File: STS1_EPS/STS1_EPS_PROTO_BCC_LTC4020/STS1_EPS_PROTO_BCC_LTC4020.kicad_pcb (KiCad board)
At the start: 2 copper layers, 47 parts, among them J1 1729267, J10 External Thermistor, J11 Terminal BAT, J9 Output, Q1 SI7135DP-T1-GE3, U1 LTC4020EUHF-PBF, U2 SI7272DP-T1-GE3, U3 SI7272DP-T1-GE3

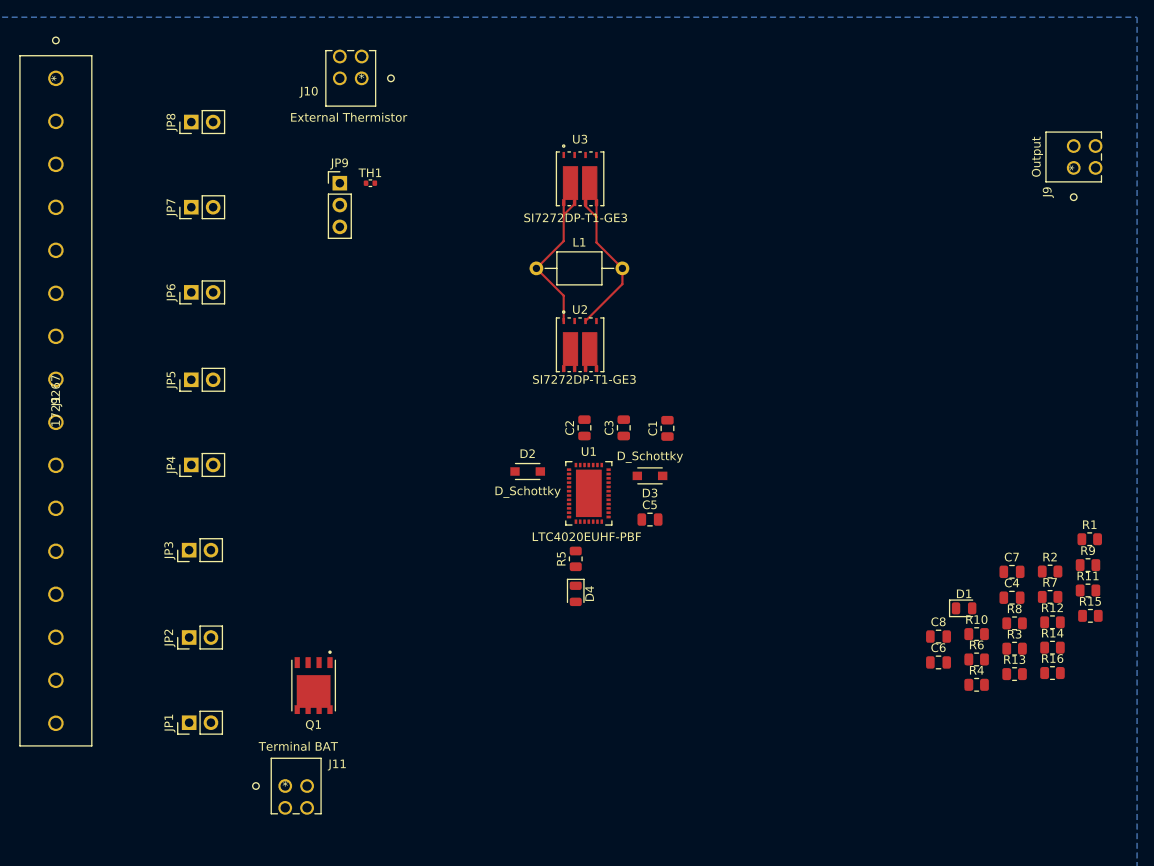
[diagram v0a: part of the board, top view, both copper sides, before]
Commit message: Re-added battery charger schematic for STS1_EPS_PROTO_BCC_LTC4020 project.
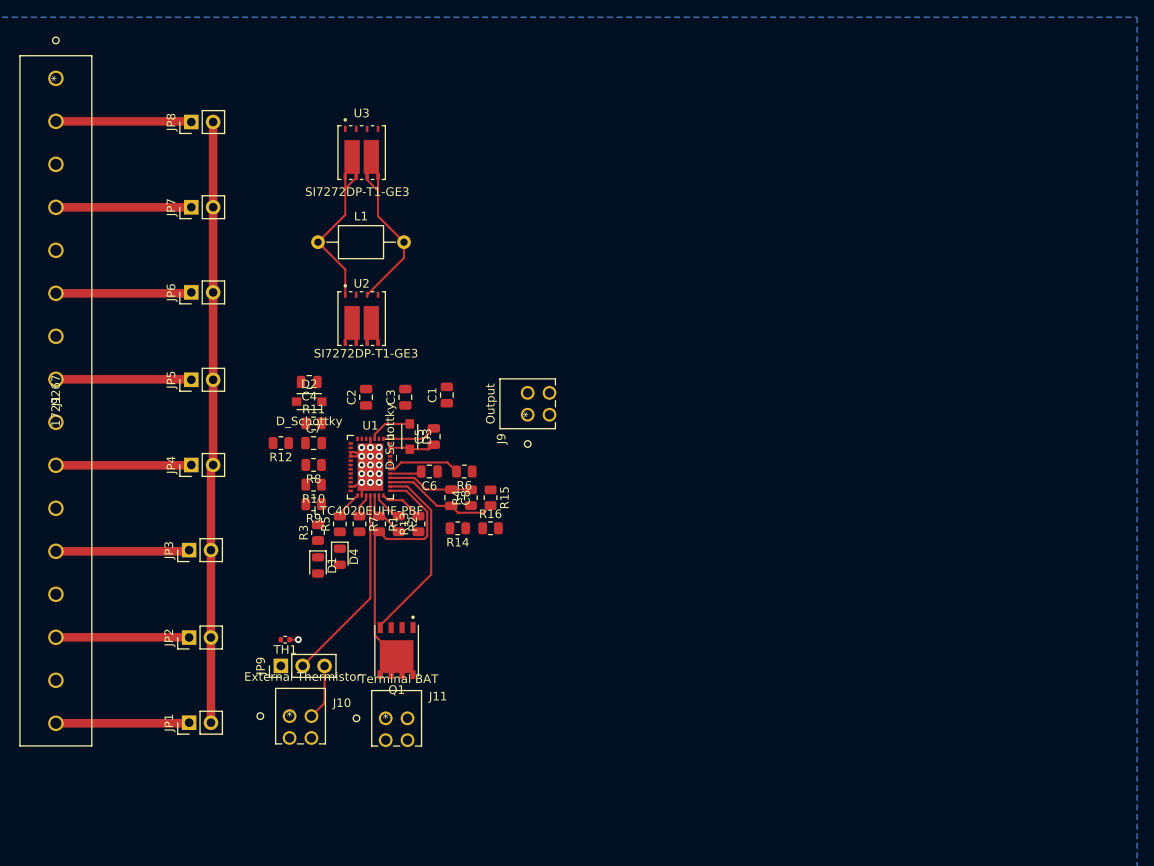
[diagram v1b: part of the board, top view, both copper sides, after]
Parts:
- moved R11 92.1 mm to (91.9, 73.7)
- moved R12 92.1 mm to (88.1, 75.9), turned to 180 degrees
- moved R9 90.3 mm to (91.9, 83.1), turned to 180 degrees
- moved C4 85.5 mm to (91.4, 68.8), turned to 180 degrees
- moved R8 83.6 mm to (91.9, 78.5), turned to 180 degrees
- moved R1 82.7 mm to (99.6, 85.3), turned to 270 degrees
- moved C7 82.6 mm to (91.9, 75.9)
- moved R3 82.1 mm to (92.5, 86.4), turned to 90 degrees
- moved R7 80.8 mm to (97.3, 85.3), turned to 270 degrees
- moved R10 79.0 mm to (91.9, 80.8), turned to 180 degrees
- moved R2 75.9 mm to (101.9, 85.3), turned to 270 degrees
- moved D1 75.3 mm to (92.5, 90.2), turned to 270 degrees
- moved J10 74.6 mm to (89.2, 107.7), turned to 0 degrees
- moved R13 71.5 mm to (104.1, 85.3), turned to 90 degrees
- moved R15 71.1 mm to (112.5, 82.3), turned to 270 degrees
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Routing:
- net /EPS Battery Charger/Vin: track 0.00 -> 70.0 mm
- net /EPS Battery Charger/BAT: track 0.00 -> 31.8 mm
- net /EPS Battery Charger/NTC: track 0.00 -> 23.1 mm
- net /EPS Battery Charger/BGATE: track 0.00 -> 22.0 mm
- net Net-(J1-Pad10): track 0.00 -> 15.8 mm
- net Net-(J1-Pad4): track 0.02 -> 15.8 mm
- net Net-(J1-Pad8): track 0.07 -> 15.8 mm
- net Net-(J1-Pad2): track 0.11 -> 15.8 mm
- net Net-(J1-Pad6): track 0.15 -> 15.8 mm
- net GND: track 0.00 -> 15.6 mm, vias 0 -> 16
- net Net-(J1-Pad12): track 0.00 -> 15.6 mm
- net Net-(J1-Pad16): track 0.00 -> 15.5 mm
- net Net-(J1-Pad14): track 0.00 -> 15.5 mm
- net /EPS Battery Charger/CSN: track 0.00 -> 13.5 mm
- net /EPS Battery Charger/CSP: track 0.00 -> 9.97 mm
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
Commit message: Worked on STS1_EPS_PROTO_BCC_LTC4020 pcb.
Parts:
- moved R16 7.62 mm to (108.0, 91.9), turned to 270 degrees
- moved R15 6.04 mm to (110.2, 87.9), turned to 90 degrees
- moved C1 2.55 mm to (104.9, 70.6)
- moved C2 2.29 mm to (100.3, 70.6)
- moved R14 2.17 mm to (108.0, 87.9), turned to 90 degrees
- moved D3 1.30 mm to (104.4, 74.9)
- moved C5 1.30 mm to (107.2, 74.9)
- moved C6 0.51 mm to (105.4, 78.7)
- moved R6 0.51 mm to (109.5, 78.7)
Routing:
- net /EPS Battery Charger/VFB: track 5.65 -> 23.1 mm, vias 0 -> 2
- net /EPS Battery Charger/Vout: track 0.00 -> 12.6 mm, vias 0 -> 2
- net /EPS Battery Charger/SW2: track 25.4 -> 19.0 mm
- net GND: track 15.6 -> 21.9 mm, vias 16 -> 20
- net /EPS Battery Charger/CSP: track 9.97 -> 16.2 mm, vias 0 -> 2
- net /EPS Battery Charger/VFBMAX: track 5.08 -> 10.8 mm, vias 0 -> 2
- net /EPS Battery Charger/BST2: track 5.36 -> 0.00 mm
- net /EPS Battery Charger/INTVCC: track 5.09 -> 0.00 mm
- net Net-(Q1-Pad1): track 0.00 -> 5.01 mm
- net /EPS Battery Charger/BAT: track 31.8 -> 36.7 mm
- net /EPS Battery Charger/CSN: track 13.5 -> 12.9 mm

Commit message: Reworked BCC
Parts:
- removed J10: External Thermistor, footprints:1725656
- added C10: 56µ, Capacitor_SMD:C_Elec_6.3x5.4, F.Cu at (89.7, 38.9)
- added C9: 56µ, Capacitor_SMD:C_Elec_6.3x5.4, F.Cu at (98.6, 38.9)
- added J4: External NTC, footprints:1725656, F.Cu at (89.4, 108.0)
- C1, C7: value C -> 100n; footprint Capacitor_SMD:C_0805_2012Metric -> Capacitor_SMD:C_1812_4532Metric
- C2: value C -> 4µ7; footprint Capacitor_SMD:C_0805_2012Metric -> Capacitor_SMD:C_1812_4532Metric
- C3: value CP -> 56µ; footprint Capacitor_SMD:C_0805_2012Metric -> Capacitor_SMD:C_Elec_6.3x5.4
- C4, C5: value C -> 1µ
- L1: value 1m -> INDUCTOR
- R11, R12: value R -> 5m; footprint Resistor_SMD:R_0805_2012Metric -> footprints:CST0612-FC-R002E
- TH1: footprint Resistor_SMD:R_0402_1005Metric -> Resistor_SMD:R_0603_1608Metric
- moved J2 32.5 mm to (116.6, 40.1)
- moved C3 32.1 mm to (107.2, 38.9)
- moved C7 26.9 mm to (91.2, 49.0), turned to 180 degrees
- moved R11 24.1 mm to (113.5, 63.0), turned to 90 degrees
- moved C1 22.9 mm to (106.4, 47.8), turned to 180 degrees
- moved R12 22.6 mm to (91.2, 53.6), turned to 0 degrees
- moved C2 18.3 mm to (106.4, 53.3), turned to 180 degrees
- moved U3 17.9 mm to (91.2, 58.9), turned to 180 degrees
- moved L1 12.4 mm to (98.3, 63.5), turned to 90 degrees
- moved U2 8.52 mm to (105.7, 58.9), turned to 180 degrees
- moved R8 4.99 mm to (87.1, 79.8), turned to 90 degrees
- moved C5 3.09 mm to (104.1, 75.4)
- moved R14 2.54 mm to (110.5, 87.9)
- moved R16 2.54 mm to (110.5, 91.9)
- moved D3 2.29 mm to (106.7, 74.9)
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- renumbered J9 to J2, J11 to J3
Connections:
- C7 pad 2: /EPS Battery Charger/SENSBOT -> Net-(C7-Pad2)
- R11 pad 2: /EPS Battery Charger/SENSTOP -> /EPS Battery Charger/Vin
- R12 pad 1: /EPS Battery Charger/SENSBOT -> Net-(C7-Pad2)
- R12 pad 2: GND -> /EPS Battery Charger/SENSBOT
- U1 pad 28: Net-(U1-Pad28) -> /EPS Battery Charger/Vin
- U1 pad 29: Net-(U1-Pad29) -> GND
- U2 pad 7: /EPS Battery Charger/SENSTOP -> Net-(R11-Pad3)
- U2 pad 8: Net-(U2-Pad8) -> Net-(R11-Pad3)
- U3 pad 1: /EPS Battery Charger/SENSBOT -> Net-(C7-Pad2)
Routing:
- net /EPS Battery Charger/Vin: track 70.0 -> 129.6 mm, vias 0 -> 5
- net GND: track 21.9 -> 74.1 mm, vias 20 -> 37
- net /EPS Battery Charger/BG2: track 0.00 -> 34.1 mm, vias 0 -> 2
- net /EPS Battery Charger/Vout: track 12.6 -> 45.2 mm
- net /EPS Battery Charger/BG1: track 0.00 -> 29.6 mm, vias 0 -> 2
- net /EPS Battery Charger/SENSBOT: track 0.00 -> 26.7 mm, vias 0 -> 2
- net /EPS Battery Charger/TG2: track 0.00 -> 22.8 mm, vias 0 -> 2
- net /EPS Battery Charger/TG1: track 0.00 -> 22.0 mm, vias 0 -> 2
- net /EPS Battery Charger/INTVCC: track 0.00 -> 14.6 mm, vias 0 -> 3
- net /EPS Battery Charger/SW1: track 18.3 -> 31.1 mm, vias 0 -> 3
- net Net-(R10-Pad1): track 0.00 -> 11.3 mm
- net Net-(Q1-Pad1): track 5.01 -> 15.5 mm
- net /EPS Battery Charger/BAT: track 36.7 -> 46.5 mm
- net /EPS Battery Charger/BST1: track 0.00 -> 9.80 mm
- net Net-(R9-Pad1): track 0.00 -> 9.56 mm, vias 0 -> 2
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- added copper zone on F.Cu, net /EPS Battery Charger/Vout
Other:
- board outline added: 63 x 81.3 mm
- net class 6A Power added: clearance 0.2, trace_width 0.25, via_dia 0.8, via_drill 0.4

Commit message: - STS1_EPS_PROTO_SCC_L6920 now uses the STS1 PCB template and is again ready for review. - WOrked on STS1_EPS_PROTO_BCC_LTC4020.
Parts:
- removed the C1 at (106.4, 47.8)
- removed the C10 at (89.7, 38.9)
- removed the C2 at (106.4, 53.3)
- removed the C3 at (107.2, 38.9)
- removed the C9 at (98.6, 38.9)
- added C1: 680µ, Capacitor_Tantalum_SMD:CP_EIA-7361-438_AVX-U, F.Cu at (289.9, 153.6)
- added C1: 100n, Capacitor_SMD:C_1812_4532Metric, F.Cu at (232.2, 128.4)
- added C10: 680p, Capacitor_SMD:C_0805_2012Metric, F.Cu at (291.7, 178.0)
- added C10: 56µ, Capacitor_SMD:C_Elec_6.3x5.4, F.Cu at (224.4, 121.9)
- added C11: 50µ, footprints:FE52N6J0506KB, F.Cu at (223.5, 78.4)
- added C12: 50µ, footprints:FE52N6J0506KB, F.Cu at (217.3, 20.7)
- added C13: 2µ2, Capacitor_SMD:C_0805_2012Metric, F.Cu at (304.9, 59.0)
- added C14: 10µ, Capacitor_SMD:C_0805_2012Metric, F.Cu at (297.7, 68.5)
- added C15: 200n, Capacitor_SMD:C_0805_2012Metric, F.Cu at (299.3, 64.3)
- added C16: 680p, Capacitor_SMD:C_0805_2012Metric, F.Cu at (287.2, 178.0)
- added C2: 100n, Capacitor_SMD:C_0805_2012Metric, F.Cu at (316.1, 91.6)
- added C2: 4µ7, Capacitor_SMD:C_1812_4532Metric, F.Cu at (222.9, 142.8)
- added C3: 680µ, Capacitor_Tantalum_SMD:CP_EIA-7361-438_AVX-U, F.Cu at (273.8, 153.6)
- added C3: 56µ, Capacitor_SMD:C_Elec_6.3x5.4, F.Cu at (234.3, 121.9)
- added C9: 100n, Capacitor_SMD:C_0805_2012Metric, F.Cu at (299.4, 91.6)
- added C9: 56µ, Capacitor_SMD:C_Elec_6.3x5.4, F.Cu at (244.3, 121.9)
- added CON1: DISCO-CON1, footprints:Cubesatconnector, B.Cu at (118.4, 86.8)
- added CON11: DISCO-CON1, footprints:Cubesatconnector, F.Cu at (118.4, 86.8)
- added CON2: DISCO-CON2, footprints:Cubesatconnector, B.Cu at (196.4, 82.8)
- added CON21: DISCO-CON2, footprints:Cubesatconnector, F.Cu at (196.4, 82.8)
- added FID1: Fiducial, Fiducial:Fiducial_0.75mm_Mask1.5mm, F.Cu at (123.4, 109.8)
- added FID2: Fiducial, Fiducial:Fiducial_0.75mm_Mask1.5mm, F.Cu at (191.4, 58.9)
- added FID3: Fiducial, Fiducial:Fiducial_0.75mm_Mask1.5mm, F.Cu at (191.4, 105.9)
- added FID4: Fiducial, Fiducial:Fiducial_0.75mm_Mask1.5mm, F.Cu at (123.4, 58.9)
- added G***: LOGO, spaceteam:STLogo, F.Cu at (135.5, 57.8)
- added H1: MountingHole_Pad, MountingHole:MountingHole_3.2mm_M3_Pad_Via, F.Cu at (119.4, 46.3)
- added H2: MountingHole_Pad, MountingHole:MountingHole_3.2mm_M3_Pad_Via, F.Cu at (195.4, 46.3)
- added H3: MountingHole_Pad, MountingHole:MountingHole_3.2mm_M3_Pad_Via, F.Cu at (119.4, 122.3)
- added H4: MountingHole_Pad, MountingHole:MountingHole_3.2mm_M3_Pad_Via, F.Cu at (195.4, 122.3)
- added J10: BG2, Connector_PinHeader_2.54mm:PinHeader_1x01_P2.54mm_Vertical, F.Cu at (244.4, 161.4)
- added J11: BGATE, Connector_PinHeader_2.54mm:PinHeader_1x01_P2.54mm_Vertical, F.Cu at (257.8, 152.1)
- added J5: VIN_REG, Connector_PinHeader_2.54mm:PinHeader_1x01_P2.54mm_Vertical, F.Cu at (244.4, 156.7)
- added J6: SHDN, Connector_PinHeader_2.54mm:PinHeader_1x01_P2.54mm_Vertical, F.Cu at (257.8, 161.4)
- added J7: TG1, Connector_PinHeader_2.54mm:PinHeader_1x01_P2.54mm_Vertical, F.Cu at (244.4, 152.1)
- added J8: TG2, Connector_PinHeader_2.54mm:PinHeader_1x01_P2.54mm_Vertical, F.Cu at (244.4, 166.0)
- added J9: BG1, Connector_PinHeader_2.54mm:PinHeader_1x01_P2.54mm_Vertical, F.Cu at (257.8, 156.7)
- added JP10: Jumper_3_Open, Connector_PinHeader_2.54mm:PinHeader_1x03_P2.54mm_Vertical, F.Cu at (281.5, 58.4)
- added JP11: Jumper_3_Open, Connector_PinHeader_2.54mm:PinHeader_1x03_P2.54mm_Vertical, F.Cu at (286.2, 48.7)
- added JP12: Jumper_3_Open, Connector_PinHeader_2.54mm:PinHeader_1x03_P2.54mm_Vertical, F.Cu at (294.7, 43.5)
- added JP13: Jumper_3_Open, Connector_PinHeader_2.54mm:PinHeader_1x03_P2.54mm_Vertical, F.Cu at (281.5, 48.7)
- added JP15: Input Voltage, Connector_PinHeader_2.54mm:PinHeader_1x02_P2.54mm_Vertical, F.Cu at (297.1, 152.1)
- added JP16: Input Current Shunt, Connector_PinHeader_2.54mm:PinHeader_1x02_P2.54mm_Vertical, F.Cu at (306.4, 152.1)
- added JP17: Output Current Shunt, Connector_PinHeader_2.54mm:PinHeader_1x02_P2.54mm_Vertical, F.Cu at (301.8, 152.1)
- added JP18: Top Side Current Shunt, Connector_PinHeader_2.54mm:PinHeader_1x02_P2.54mm_Vertical, F.Cu at (262.5, 166.0)
- added JP19: Low Side Current Shunt, Connector_PinHeader_2.54mm:PinHeader_1x02_P2.54mm_Vertical, F.Cu at (271.2, 159.7)
- added JP20: Battery Current, Connector_PinHeader_2.54mm:PinHeader_1x02_P2.54mm_Vertical, F.Cu at (257.8, 166.0)
- added JP21: Jumper_3_Open, Connector_PinHeader_2.54mm:PinHeader_1x03_P2.54mm_Vertical, F.Cu at (287.3, 169.1)
- added JP22: Jumper_3_Open, Connector_PinHeader_2.54mm:PinHeader_1x03_P2.54mm_Vertical, F.Cu at (292.0, 169.1)
- added R17: 31k, Resistor_SMD:R_0805_2012Metric, F.Cu at (294.3, 73.5)
- added R18: 100k, Resistor_SMD:R_0805_2012Metric, F.Cu at (294.3, 76.4)
- added R19: 10m, footprints:CST0612-FC-R002E, F.Cu at (286.0, 58.6)
- added R20: 5m, footprints:CST0612-FC-R002E, F.Cu at (311.7, 92.6)
- added R21: 600k, footprints:TS53YL 20K 20&percent_, F.Cu at (328.3, 61.6)
- added R22: 200k, Resistor_SMD:R_0805_2012Metric, F.Cu at (299.4, 94.6)
- added R23: 50k, footprints:TS53YL 20K 20&percent_, F.Cu at (347.2, 61.6)
- added R24: 50k, footprints:TS53YL 20K 20&percent_, F.Cu at (353.7, 61.6)
- added R25: 5m, footprints:CST0612-FC-R002E, F.Cu at (287.1, 159.9)
- added REF**: MountingHole_3.2mm_M3, Mounting_Holes:MountingHole_3.2mm_M3, F.Cu at (195.4, 46.3)
- added U4: coordinate_system, footprints:Coordinates, F.Cu at (180.4, 48.7)
- C6: value C -> 100p
- C7: value 100n -> 200n
- C8: value C -> 330n
- L1: value INDUCTOR -> 680n; footprint Inductor_THT:L_Axial_L5.0mm_D3.6mm_P10.00mm_Horizontal_Murata_BL01RN1A2A2 -> footprints:INDPM7366X500N
- R1: value R -> 28k
- R10: value R -> 200k
- R13: value R -> 17k8
- R14, R15: value R -> 100
- R16, R2: value R -> 100k
- R3, R5: value R -> 1k
- R4, R7: value R -> 25k
- R6: value R -> 44k
- R8: value R -> 200k; footprint Resistor_SMD:R_0805_2012Metric -> footprints:TS53YL 20K 20&percent_
- R9: value R -> 500k
- moved JP8 238.7 mm to (305.4, 110.5), turned to 0 degrees
- moved R5 234.4 mm to (325.5, 42.7), turned to 0 degrees
- moved R10 232.5 mm to (321.2, 45.7), turned to 0 degrees
- moved JP2 228.5 mm to (305.4, 117.7), turned to 0 degrees
- moved R9 225.7 mm to (314.8, 50.8), turned to 0 degrees
- moved D4 225.7 mm to (316.8, 47.8), turned to 0 degrees
- moved TH1 223.5 mm to (309.0, 61.8), turned to 0 degrees
- moved J4 221.1 mm to (301.4, 45.1)
- moved R16 220.1 mm to (325.6, 45.6), turned to 0 degrees
- moved D2 219.4 mm to (309.8, 49.6), turned to 0 degrees
- moved R8 218.2 mm to (303.7, 53.3), turned to 0 degrees
- moved C4 218.2 mm to (309.2, 55.7), turned to 0 degrees
- moved C8 216.8 mm to (321.1, 42.7), turned to 0 degrees
- moved R1 216.4 mm to (313.6, 53.7), turned to 0 degrees
- moved R14 214.4 mm to (321.2, 48.6), turned to 0 degrees
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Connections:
- net Net-(R10-Pad1) renamed /EPS Battery Charger/VIN_REG
- D1 pad 2: /EPS Battery Charger/Vin -> /EPS Battery Charger/Vout
- D4 pad 2: /EPS Battery Charger/Vin -> /EPS Battery Charger/Vout
- J2 pad 1: /EPS Battery Charger/Vout -> Net-(C1-Pad1)
- JP1 pad 2: /EPS Battery Charger/Vin -> Net-(JP1-Pad2)
- JP2 pad 2: /EPS Battery Charger/Vin -> Net-(JP1-Pad2)
- JP3 pad 2: /EPS Battery Charger/Vin -> Net-(JP1-Pad2)
- JP4 pad 2: /EPS Battery Charger/Vin -> Net-(JP1-Pad2)
- JP5 pad 2: /EPS Battery Charger/Vin -> Net-(JP1-Pad2)
- JP6 pad 2: /EPS Battery Charger/Vin -> Net-(JP1-Pad2)
- JP7 pad 2: /EPS Battery Charger/Vin -> Net-(JP1-Pad2)
- JP8 pad 2: /EPS Battery Charger/Vin -> Net-(JP1-Pad2)
- R1 pad 1: /EPS Battery Charger/VFB -> Net-(JP11-Pad3)
- R1 pad 2: /EPS Battery Charger/BAT -> /EPS Battery Charger/VFB
- R11 pad 2: /EPS Battery Charger/Vin -> /EPS Battery Charger/SENSVIN
- R13 pad 1: /EPS Battery Charger/Vout -> /EPS Battery Charger/CSP
- R13 pad 2: /EPS Battery Charger/VFBMAX -> /EPS Battery Charger/VFBMIN
- R14 pad 1: /EPS Battery Charger/Vout -> Net-(JP20-Pad2)
- R15 pad 1: Net-(Q1-Pad1) -> Net-(JP20-Pad1)
- R16 pad 1: /EPS Battery Charger/Vout -> /EPS Battery Charger/VFBMIN
- R16 pad 2: Net-(Q1-Pad1) -> /EPS Battery Charger/FBG
- R4 pad 1: /EPS Battery Charger/VFB -> GND
- R4 pad 2: /EPS Battery Charger/CSP -> Net-(JP10-Pad1)
- R6 pad 1: /EPS Battery Charger/Vin -> Net-(JP11-Pad1)
- R6 pad 2: /EPS Battery Charger/ILIMIT -> /EPS Battery Charger/VFB
- R7 pad 1: Net-(R7-Pad1) -> GND
- R7 pad 2: /EPS Battery Charger/Vin -> Net-(JP12-Pad1)
- R9 pad 1: Net-(R9-Pad1) -> GND
- R9 pad 2: GND -> /EPS Battery Charger/RT
- U1 pad 14: GND -> /EPS Battery Charger/TIMER
- U1 pad 15: Net-(R7-Pad1) -> /EPS Battery Charger/RNGSS
- U1 pad 19: /EPS Battery Charger/VFBMAX -> /EPS Battery Charger/VFBMIN
- U1 pad 28: /EPS Battery Charger/Vin -> Net-(U1-Pad28)
- U1 pad 7: /EPS Battery Charger/Vin -> /EPS Battery Charger/SENSVIN
- U1 pad 8: Net-(R9-Pad1) -> /EPS Battery Charger/RT
- U1 pad 9: /EPS Battery Charger/Vin -> /EPS Battery Charger/SHDN
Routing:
- net /EPS Battery Charger/Vin: track 129.6 -> 0.00 mm, vias 5 -> 0
- net GND: track 74.1 -> 0.00 mm, vias 37 -> 35
- net /EPS Battery Charger/BAT: track 46.5 -> 0.00 mm
- net /EPS Battery Charger/Vout: track 45.2 -> 0.00 mm, vias 2 -> 0
- net /EPS Battery Charger/BG2: track 34.1 -> 0.00 mm, vias 2 -> 0
- net /EPS Battery Charger/SW1: track 31.1 -> 0.00 mm, vias 3 -> 0
- net /EPS Battery Charger/BG1: track 29.6 -> 0.00 mm, vias 2 -> 0
- net /EPS Battery Charger/SENSBOT: track 26.7 -> 0.00 mm, vias 2 -> 0
- net /EPS Battery Charger/SW2: track 23.6 -> 0.00 mm, vias 4 -> 0
- net /EPS Battery Charger/NTC: track 23.6 -> 0.00 mm
- net /EPS Battery Charger/TG2: track 22.8 -> 0.00 mm, vias 2 -> 0
- net /EPS Battery Charger/VFB: track 22.1 -> 0.00 mm, vias 2 -> 0
- net /EPS Battery Charger/BGATE: track 22.0 -> 0.00 mm
- net /EPS Battery Charger/TG1: track 22.0 -> 0.00 mm, vias 2 -> 0
- net /EPS Battery Charger/CSP: track 18.9 -> 0.00 mm, vias 2 -> 0
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- removed copper zone on F.Cu, net /EPS Battery Charger/Vout
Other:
- board size 63 x 81.3 mm -> 85 x 85 mm
- board text added: "TU Wien Space Team STS STS1_EPS_PROTO_BCC_LTC4020 1.0.0"

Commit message: Intermediate state.
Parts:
- removed the C1 at (289.9, 153.6)
- removed the C1 at (232.2, 128.4)
- removed the C10 at (224.4, 121.9)
- removed the C2 at (222.9, 142.8)
- removed the C3 at (234.3, 121.9)
- removed the C9 at (299.4, 91.6)
- removed the C9 at (244.3, 121.9)
- added C1: 680µ, Capacitor_Tantalum_SMD:CP_EIA-7361-438_AVX-U, F.Cu at (145.6, 64.7)
- added C9: 100n, Capacitor_SMD:C_0805_2012Metric, F.Cu at (157.6, 78.4)
- C11, C12: value 50µ -> 220µ; footprint footprints:FE52N6J0506KB -> Capacitor_Tantalum_SMD:CP_EIA-3528-12_Kemet-T
- J1: footprint footprints:1729267 -> footprints:1984756
- J2: footprint footprints:1725656 -> footprints:1888807
- moved C8 189.3 mm to (134.5, 74.8), turned to 180 degrees
- moved TH1 186.4 mm to (127.6, 104.3), turned to 180 degrees
- moved J4 181.6 mm to (125.8, 91.6), turned to 270 degrees
- moved R1 180.7 mm to (137.3, 93.1), turned to 180 degrees
- moved R5 177.9 mm to (154.8, 92.9), turned to 90 degrees
- moved R24 177.6 mm to (178.3, 89.0)
- moved JP16 176.3 mm to (136.5, 105.0), turned to 180 degrees
- moved JP9 174.4 mm to (124.0, 104.3), turned to 180 degrees
- moved R6 173.9 mm to (133.7, 93.1)
- moved JP17 172.7 mm to (156.6, 58.6), turned to 270 degrees
- moved R16 171.4 mm to (160.9, 92.9), turned to 270 degrees
- moved JP8 169.4 mm to (136.0, 112.9), turned to 180 degrees
- moved C2 169.2 mm to (148.2, 70.6)
- moved R9 166.6 mm to (152.0, 86.2)
- moved R10 164.7 mm to (165.7, 100.0), turned to 270 degrees
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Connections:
- C11 pad 1: Net-(C11-Pad1) -> GND
- C11 pad 2: Net-(C11-Pad1) -> Net-(C11-Pad2)
- C12 pad 1: Net-(C12-Pad1) -> GND
- C12 pad 2: Net-(C12-Pad1) -> Net-(C12-Pad2)
- JP10 pad 3: Net-(C11-Pad1) -> Net-(C11-Pad2)
- JP12 pad 3: Net-(C12-Pad1) -> Net-(C12-Pad2)
- U1 pad 27: Net-(U1-Pad27) -> /EPS Battery Charger/ITH
- U1 pad 28: Net-(U1-Pad28) -> /EPS Battery Charger/VC
- U1 pad 36: /EPS Battery Charger/Vin -> /EPS Battery Charger/PVIN
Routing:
- net Net-(JP1-Pad2): track 0.00 -> 54.9 mm
- net GND: track 0.00 -> 13.7 mm, vias 35 -> 57
- net Net-(JP20-Pad1): track 0.00 -> 9.06 mm
- net /EPS Battery Charger/BAT: track 0.00 -> 7.90 mm
- net /EPS Battery Charger/BGATE: track 0.00 -> 7.71 mm
- net Net-(J1-Pad8): track 0.00 -> 7.67 mm
- net Net-(J1-Pad12): track 0.00 -> 7.66 mm
- net Net-(J1-Pad4): track 0.00 -> 7.66 mm
- net Net-(J1-Pad16): track 0.00 -> 7.65 mm
- net Net-(J1-Pad2): track 0.00 -> 7.64 mm
- net Net-(J1-Pad14): track 0.00 -> 7.63 mm
- net Net-(J1-Pad6): track 0.00 -> 7.63 mm
- net Net-(J1-Pad10): track 0.00 -> 7.62 mm
- net /EPS Battery Charger/Vin: track 0.00 -> 6.98 mm
- net Net-(J4-Pad2): track 0.00 -> 5.82 mm
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- added copper zone on F.Cu, net Net-(JP1-Pad2)
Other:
- board text added: "Charging"
- board text added: "Fault"

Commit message: Intermediate state.
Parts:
- removed G***: LOGO, spaceteam:STLogo
- removed JP19: Low Side Current Shunt, Connector_PinHeader_2.54mm:PinHeader_1x02_P2.54mm_Vertical
- added JP14: Low Side Current Shunt, Connector_PinHeader_2.54mm:PinHeader_1x02_P2.54mm_Vertical, F.Cu at (186.5, 78.1)
- added U5: logo, footprints:STLogoTiny, F.Cu at (133.1, 55.4)
- U2, U3: footprint footprints:SI7272DP-T1-GE3 -> footprints:SI7288DPT1GE3
- moved C4 26.3 mm to (176.1, 70.2), turned to 90 degrees
- moved J10 20.7 mm to (187.8, 57.0)
- moved J9 20.5 mm to (194.9, 59.1)
- moved R12 19.3 mm to (168.2, 70.3), turned to 90 degrees
- moved R11 19.1 mm to (186.8, 69.5), turned to 180 degrees
- moved JP18 18.5 mm to (160.4, 70.2), turned to 90 degrees
- moved C5 17.4 mm to (178.1, 57.0)
- moved C9 14.0 mm to (144.9, 84.2), turned to 0 degrees
- moved J7 13.7 mm to (172.4, 70.2)
- moved JP17 11.8 mm to (152.1, 69.4), turned to 90 degrees
- moved C7 9.12 mm to (190.5, 70.3), turned to 90 degrees
- moved U3 8.36 mm to (189.6, 63.6), turned to 180 degrees
- moved JP22 7.47 mm to (182.5, 81.2)
- moved J8 7.19 mm to (172.1, 57.0)
- moved C14 5.64 mm to (155.3, 78.4), turned to 270 degrees
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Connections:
- C7 pad 2: Net-(C7-Pad2) -> /EPS Battery Charger/switch_bridge/BOTTOM_LEFT
- R11 pad 1: /EPS Battery Charger/Vin -> /EPS Battery Charger/switch_bridge/BOTTOM_LEFT
- R11 pad 2: /EPS Battery Charger/SENSVIN -> /EPS Battery Charger/SENSBOT
- R11 pad 3: Net-(R11-Pad3) -> GND
- R11 pad 4: /EPS Battery Charger/SENSTOP -> GND
- R12 pad 1: Net-(C7-Pad2) -> /EPS Battery Charger/Vin
- R12 pad 2: /EPS Battery Charger/SENSBOT -> /EPS Battery Charger/SENSVIN
- R12 pad 3: GND -> /EPS Battery Charger/switch_bridge/TOP_LEFT
- R12 pad 4: GND -> /EPS Battery Charger/SENSTOP
- U2 pad 7: Net-(R11-Pad3) -> /EPS Battery Charger/switch_bridge/TOP_LEFT
- U2 pad 8: Net-(R11-Pad3) -> /EPS Battery Charger/switch_bridge/TOP_LEFT
- U3 pad 1: Net-(C7-Pad2) -> /EPS Battery Charger/switch_bridge/BOTTOM_LEFT
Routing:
- net /EPS Battery Charger/Vin: track 6.98 -> 105.6 mm, vias 0 -> 2
- net /EPS Battery Charger/BG1: track 0.00 -> 59.3 mm, vias 0 -> 4
- net /EPS Battery Charger/BST2: track 0.00 -> 52.5 mm, vias 0 -> 4
- net /EPS Battery Charger/NTC: track 0.00 -> 51.9 mm, vias 0 -> 2
- net /EPS Battery Charger/BG2: track 0.00 -> 50.1 mm, vias 0 -> 3
- net /EPS Battery Charger/Vout: track 0.00 -> 47.7 mm
- net /EPS Battery Charger/SW1: track 0.00 -> 44.1 mm, vias 0 -> 6
- net /EPS Battery Charger/TG2: track 0.00 -> 39.0 mm, vias 0 -> 3
- net /EPS Battery Charger/CSN: track 0.00 -> 38.5 mm, vias 0 -> 2
- net /EPS Battery Charger/SW2: track 0.00 -> 38.2 mm, vias 0 -> 4
- net /EPS Battery Charger/BAT: track 7.90 -> 46.0 mm, vias 0 -> 1
- net /EPS Battery Charger/TG1: track 0.00 -> 36.8 mm, vias 0 -> 3
- net /EPS Battery Charger/BST1: track 0.00 -> 35.5 mm, vias 0 -> 4
- net /EPS Battery Charger/VFB: track 1.73 -> 34.3 mm, vias 0 -> 2
- net /EPS Battery Charger/BGATE: track 7.71 -> 38.6 mm, vias 0 -> 2
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- added copper zone on F.Cu, net /EPS Battery Charger/SW1
- added copper zone on F.Cu, net /EPS Battery Charger/SW2
- added copper zone on B.Cu, net /EPS Battery Charger/TG1
- added copper zone on F.Cu, net /EPS Battery Charger/Vin
- added copper zone on F.Cu, net /EPS Battery Charger/Vout
- added copper zone on F.Cu, net /EPS Battery Charger/switch_bridge/BOTTOM_LEFT
- added copper zone on F.Cu, net /EPS Battery Charger/switch_bridge/TOP_LEFT
- added copper zone on F.Cu, net GND
- added copper zone on F.Cu, net Net-(C1-Pad1)
- added copper zone on F.Cu, net Net-(Q1-Pad1)
